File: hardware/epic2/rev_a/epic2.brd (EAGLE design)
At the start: 18.8 x 19.6 mm, 35 parts, among them J1 EPIC2-HEADER2, U2 FM25LBTDFN-8, U3 CC2538, U5 RV-3049-C3, X1 EPSON-FA-128, X3 ABS05-32.768KHZ-T

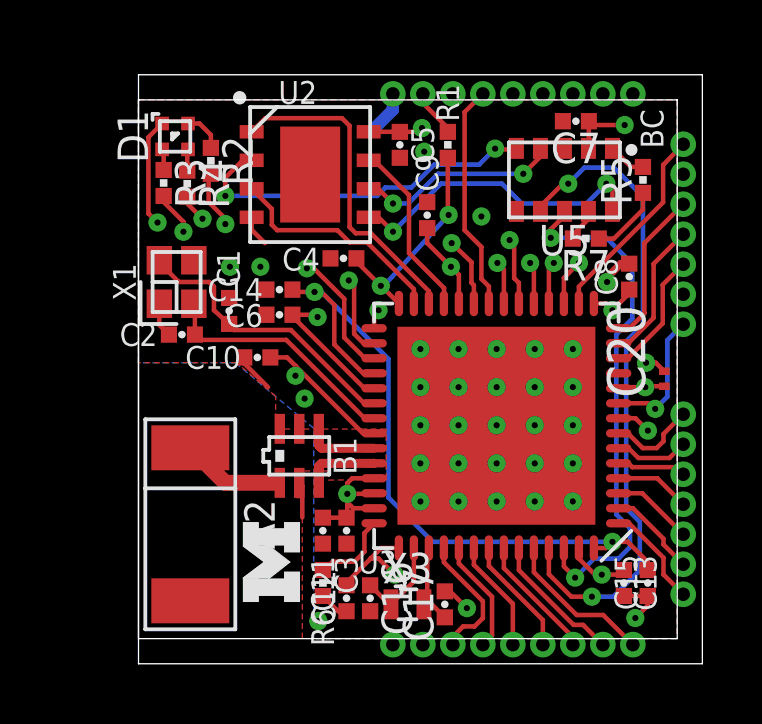
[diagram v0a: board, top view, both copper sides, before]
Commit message: moved castellated headers in
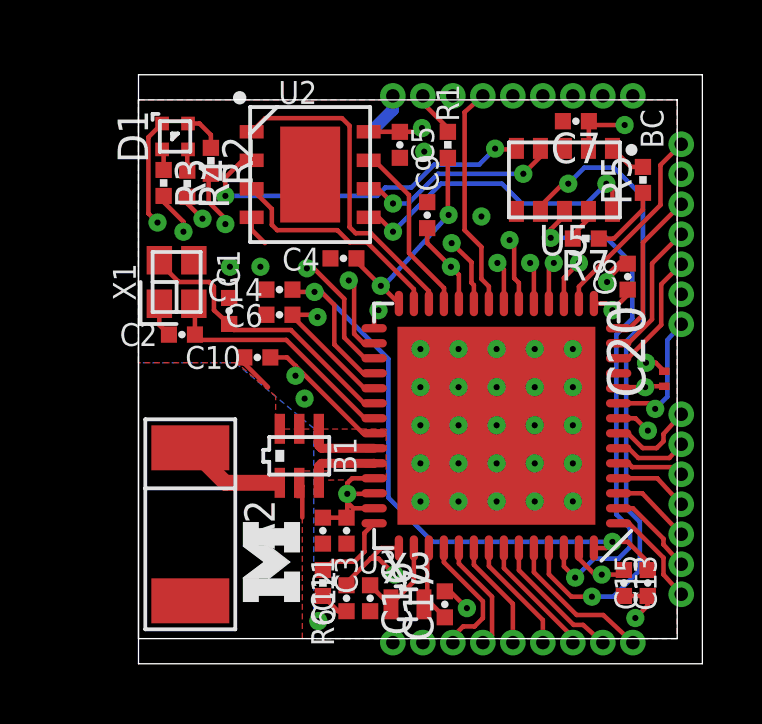
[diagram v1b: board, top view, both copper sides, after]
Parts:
- moved C8 0.05 mm to (16.3, 12.1)

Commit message: rerouted after moving castellated headers
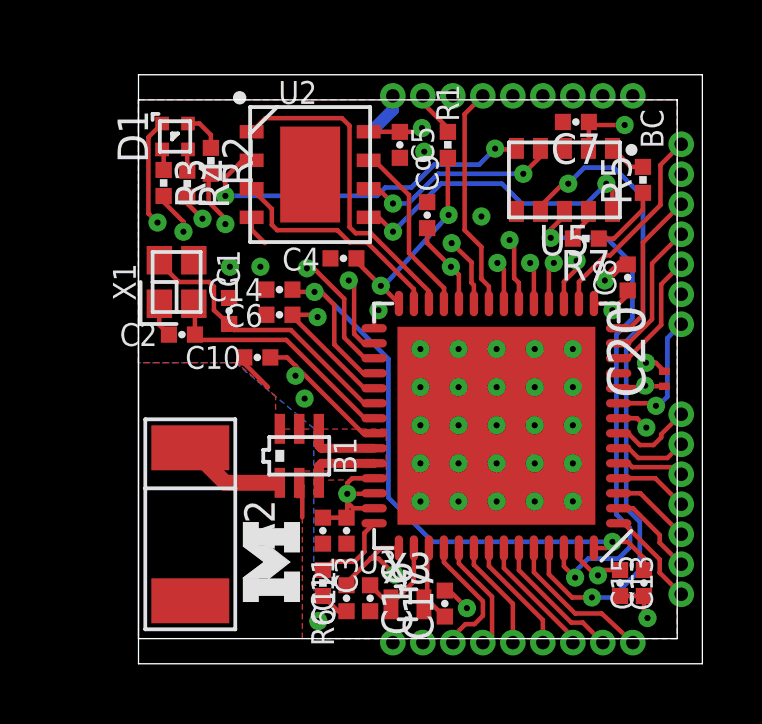
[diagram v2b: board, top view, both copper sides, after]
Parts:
- moved C13 0.13 mm to (16.1, 1.85)
- moved C15 0.13 mm to (16.8, 1.85)
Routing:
- net DGND_USB: track 3.41 -> 3.99 mm

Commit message: epic2/myth routed
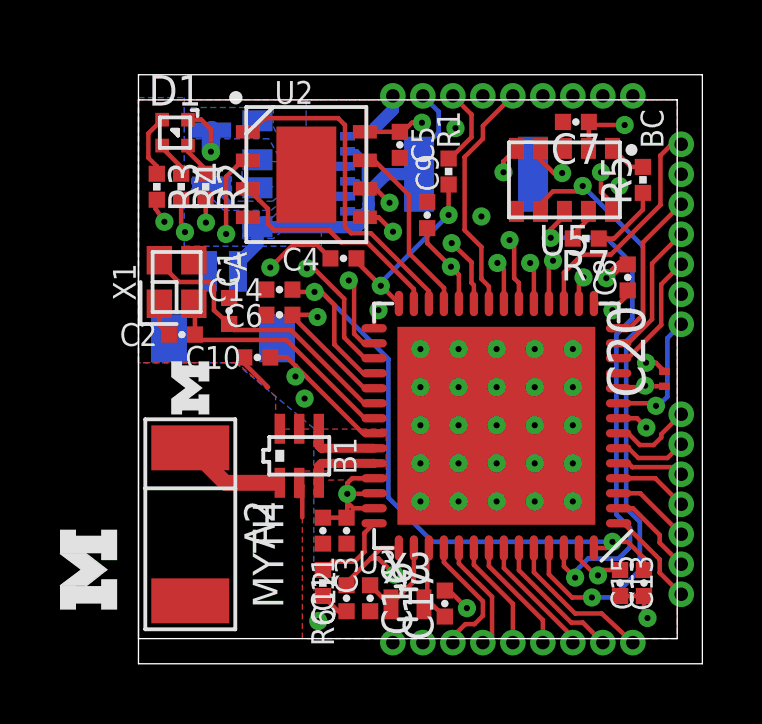
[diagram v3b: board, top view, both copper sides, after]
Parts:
- added BT1: ML-1220/F1AN, batteries:ML-1220/F1BN
- added C18, C19: 10uF, passives:0603_CAP
- added J2: SH_MALE_2/1MM, headers:SH-1X2/1MM
- added L1: 2.2, passives:MIPSZ201D
- added LOGO1: UMICH_SOLID_TINY, logos:UMICH_SOLID_50MIL
- added U1: TPS62740, chips:R-PWSON-12
- moved U$1 6.10 mm to (-0.71, 0.97)
- moved R1 0.89 mm to (10.3, 15.6)
- moved R2 0.88 mm to (2.24, 15.1)
- moved R3 0.26 mm to (0.61, 15.1)
- moved R4 0.23 mm to (1.42, 15.1)
- moved U2 0.13 mm to (5.60, 15.5)
- moved D1 0.13 mm to (1.22, 16.9), turned to 0 degrees
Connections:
- removed net UNUSED2: J1.22
- new net BATTERY: BT1.POS, C18.1, J1.31, J2.2, U1.1, U1.10, U1.12, U1.8
- new net N$5: L1.1, U1.2
- net !RESET: now also J1.30; no longer J1.31
- net ADC3: now also J1.25; no longer J1.26
- net ADC4: now also J1.26; no longer J1.27
- net ADC5: now also J1.27; no longer J1.28
- net ADC6: now also J1.28; no longer J1.29
- net ADC7: now also J1.29; no longer J1.30
- net BOOTLOADER_CTRL: now also J1.24; no longer J1.25
- net BOOTLOADER_RX: now also J1.22; no longer J1.23
- net BOOTLOADER_TX: now also J1.23; no longer J1.24
- net GND: now also BT1.NEG, C18.2, C19.2, J2.1, U1.11, U1.3, U1.4, U1.9, U1.NC
- net VCC: now also C19.1, L1.2, U1.5
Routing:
- net BATTERY: track 0.00 -> 14.7 mm
- net VCC: track 34.5 -> 39.4 mm
- net GND: track 15.1 -> 19.5 mm
- net SPI_SCK: track 25.8 -> 27.6 mm
- net SPI_MISO: track 35.0 -> 36.6 mm
- net !RTC_INT: track 22.0 -> 20.6 mm
- net N$11: track 0.71 -> 2.11 mm
- net LED_GREEN: track 10.3 -> 11.6 mm
- net LED_BLUE: track 9.47 -> 10.6 mm
- net !RESET: track 1.54 -> 2.69 mm
- net BOOTLOADER_CTRL: track 8.21 -> 9.30 mm
- net N$5: track 0.00 -> 1.01 mm
- net N$1: track 7.36 -> 6.40 mm
- net BOOTLOADER_RX: track 6.81 -> 5.94 mm, vias 0 -> 1
- net ADC3: track 7.69 -> 8.42 mm
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- added copper zone on layer 16, net BATTERY
- added copper zone on layer 16, net N$5
- added copper zone on layer 16, net VCC
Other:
- board text added: "+"
- board text added: "-"
- board text added: "A"
- board text added: "MYTH"

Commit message: updated epic2 brd
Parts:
- removed U$1: UMICH_SOLID_SMALL, logos:UMICH_SOLID_75MIL
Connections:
- net !RTC_CS renamed RTC_CE
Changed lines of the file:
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@@
 <layers>
 <layer number="1" name="Top" color="4" fill="1" visible="yes" active="yes"/>
-<layer number="2" name="Route2" color="13" fill="10" visible="no" active="yes"/>
+<layer number="2" name="Route2" color="13" fill="10" visible="yes" active="yes"/>
 <layer number="3" name="Route3" color="4" fill="3" visible="no" active="no"/>
 <layer number="4" name="Route4" color="1" fill="4" visible="no" active="no"/>
@@
 <layer number="13" name="Route13" color="4" fill="5" visible="no" active="no"/>
 <layer number="14" name="Route14" color="1" fill="6" visible="no" active="no"/>
-<layer number="15" name="Route15" color="3" fill="6" visible="no" active="yes"/>
-<layer number="16" name="Bottom" color="1" fill="1" visible="no" active="yes"/>
+<layer number="15" name="Route15" color="3" fill="6" visible="yes" active="yes"/>
+<layer number="16" name="Bottom" color="1" fill="1" visible="yes" active="yes"/>
 <layer number="17" name="Pads" color="2" fill="1" visible="yes" active="yes"/>
 <layer number="18" name="Vias" color="2" fill="1" visible="yes" active="yes"/>
@@
 <layer number="50" name="dxf" color="7" fill="1" visible="no" active="no"/>
 <layer number="51" name="tDocu" color="14" fill="1" visible="yes" active="yes"/>
-<layer number="52" name="bDocu" color="14" fill="1" visible="no" active="yes"/>
+<layer number="52" name="bDocu" color="14" fill="1" visible="yes" active="yes"/>
 <layer number="53" name="tGND_GNDA" color="7" fill="9" visible="no" active="no"/>
 <layer number="54" name="bGND_GNDA" color="1" fill="9" visible="no" active="no"/>
@@
 </autorouter>
 <elements>
-<element name="U$1" library="logos" package="UMICH_SOLID_75MIL" value="UMICH_SOLID_SMALL" x="-0.7112" y="0.9652" rot="R90"/>
 <element name="U2" library="chips" package="TDFN-8" value="FM25LBTDFN-8" x="5.5954" y="15.469" smashed="yes" rot="R270">
 <attribute name="DIGIKEY" value="FM25L04B-DGRA-ND" x="5.5954" y="15.469" size="1.778" layer="27" rot="R270" display="off"/>
@@
 <wire x1="5.0292" y1="12.9286" x2="5.6134" y2="12.3444" width="0.1524" layer="15"/>
 <wire x1="3.5052" y1="12.3444" x2="1.3716" y2="12.3444" width="0.1524" layer="15"/>
-<wire x1="0.6096" y1="14.62913125" x2="0.5588" y2="14.34973125" width="0.1524" layer="1"/>
-<wire x1="0.5588" y1="14.34973125" x2="0.8636" y2="13.8938" width="0.1524" layer="1"/>
 <wire x1="1.3716" y1="12.3444" x2="0.8636" y2="12.8524" width="0.1524" layer="15"/>
 <wire x1="0.8636" y1="12.8524" x2="0.8636" y2="13.8938" width="0.1524" layer="15"/>
+<wire x1="0.6096" y1="14.62913125" x2="0.6096" y2="14.1478" width="0.1524" layer="1"/>
+<wire x1="0.6096" y1="14.1478" x2="0.8636" y2="13.8938" width="0.1524" layer="1"/>
 </signal>
 <signal name="LED_RED">
@@
 <wire x1="16.41553125" y1="15.72386875" x2="15.7986" y2="16.3408" width="0.1524" layer="1"/>
 </signal>
-<signal name="!RTC_CS">
+<signal name="RTC_CE">
 <contactref element="U5" pad="8"/>
 <via x="14.5542" y="2.032" extent="1-16" drill="0.2032"/>
